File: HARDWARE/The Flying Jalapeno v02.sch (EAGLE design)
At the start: 96 parts, among them Q2 MMBT2222A, Q3 NDP6020P, Q4 MMBT2222A, Q5 NDP6020P, Q6 BSS138, 200mA/50V, Q7 BSS138, 200mA/50V, U1 ATMEGA2560AU, U2 LM1117, U3 LM1117, U4 LM1117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

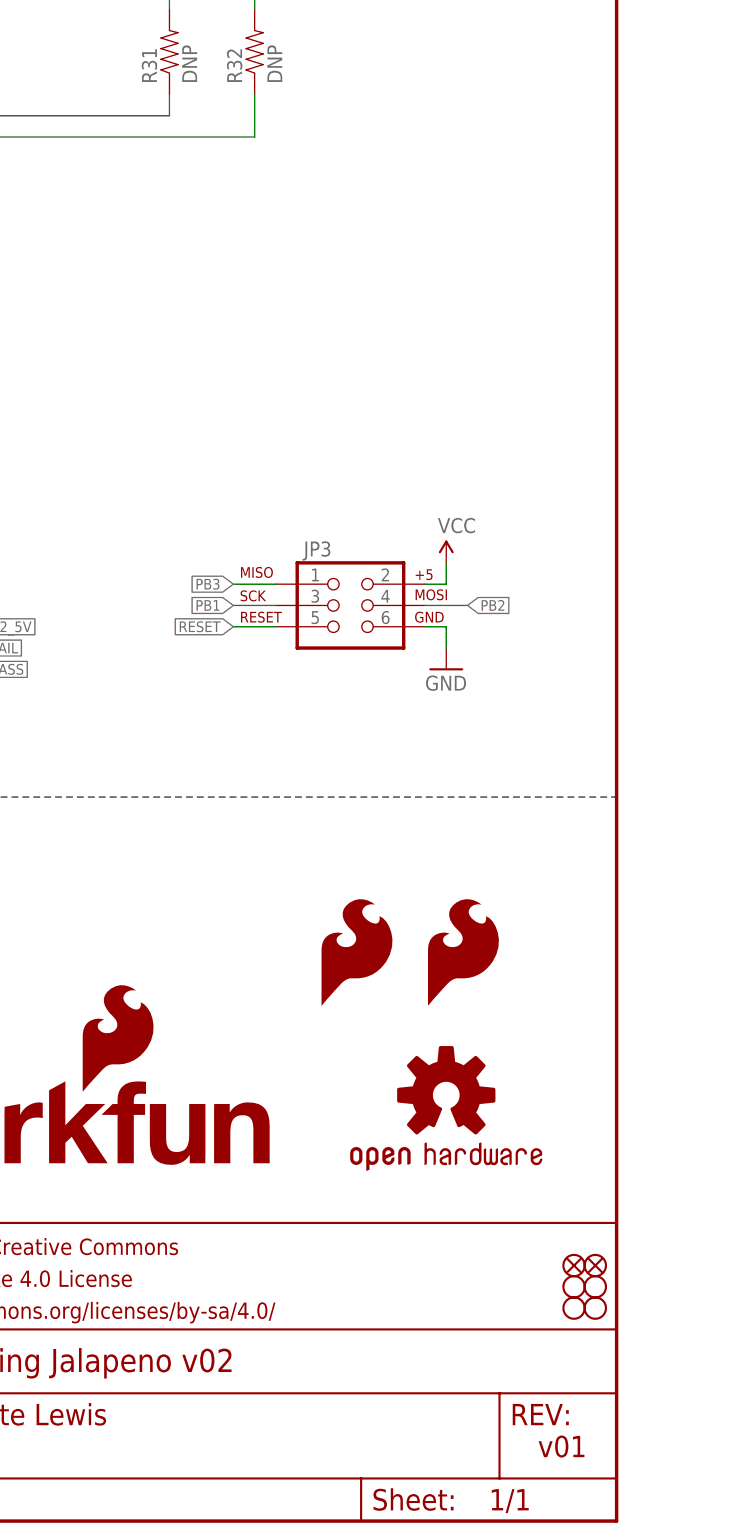
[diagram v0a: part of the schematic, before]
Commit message: added in PCA9306 for I2C - still not netted or routed
also added ignore for lock files
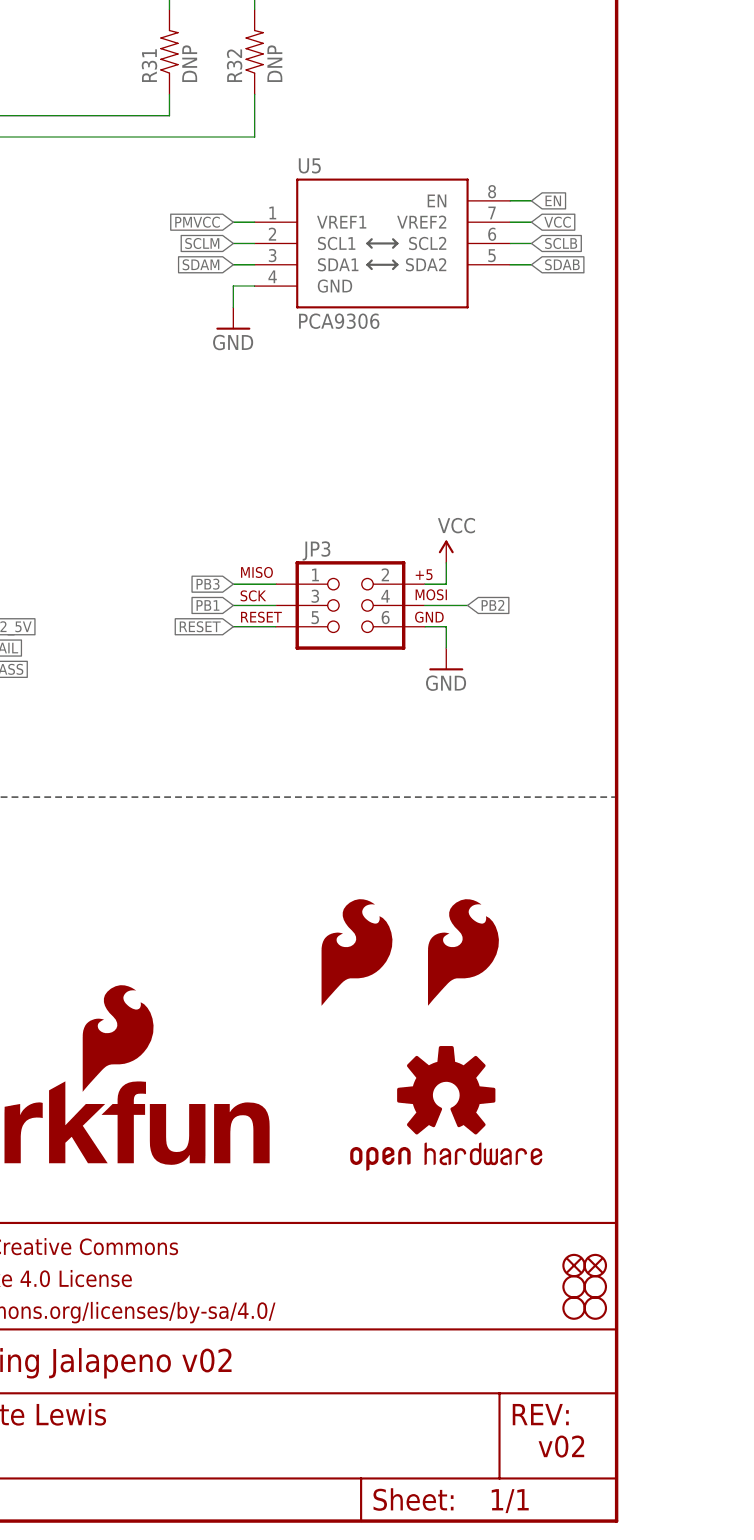
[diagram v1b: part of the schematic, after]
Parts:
- added U5: PCA9306, SparkFun-DigitalIC:PCA9306PCA9306DC-1:1
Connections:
- new net EN: U5.EN
- new net PMVCC: U5.VREF1
- new net SCLB: U5.SCL2
- new net SCLM: U5.SCL1
- new net SDAB: U5.SDA2
- new net SDAM: U5.SDA1
- net GND: now also U5.GND
- net VCC: now also U5.VREF2
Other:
- note added: "v02"
- note removed: "v01"
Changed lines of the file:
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@@
 <?xml version="1.0" encoding="utf-8"?>
 <!DOCTYPE eagle SYSTEM "eagle.dtd">
-<eagle version="7.3.0">
+<eagle version="7.5.0">
 <drawing>
 <settings>
@@
 <layer number="113" name="IDFDebug" color="4" fill="1" visible="yes" active="yes"/>
 <layer number="114" name="Badge_Outline" color="11" fill="1" visible="no" active="no"/>
+<layer number="115" name="ReferenceISLANDS" color="7" fill="1" visible="yes" active="yes"/>
 <layer number="116" name="Patch_BOT" color="9" fill="4" visible="yes" active="yes"/>
 <layer number="118" name="Rect_Pads" color="7" fill="1" visible="yes" active="yes"/>
@@
 </class>
 <class number="2" name="POWER" width="0.2032" drill="0">
+</class>
+<class number="10" name="12_mil" width="0.3048" drill="0.381">
+</class>
+<class number="11" name="15_mil" width="0.381" drill="0.381">
 </class>
 </classes>
@@
 <part name="R40" library="SparkFun-Resistors" deviceset="470OHM1/10W1%(0603)" device="" value="470"/>
 <part name="LOGO2" library="SparkFun-Aesthetics" deviceset="SFE_LOGO_FLAME" device=".3_INCH"/>
+<part name="U5" library="SparkFun-DigitalIC" deviceset="PCA9306" device="PCA9306DC-1:1" value="PCA9306"/>
+<part name="GND7" library="SparkFun" deviceset="GND" device=""/>
 </parts>
 <sheets>
@@
 <text x="200.66" y="269.24" size="3.81" layer="97">MICRO</text>
 <text x="354.33" y="11.43" size="2.54" layer="94">Pete Lewis</text>
-<text x="422.402" y="7.62" size="2.54" layer="94">v01</text>
+<text x="422.402" y="7.62" size="2.54" layer="94">v02</text>
 <text x="144.78" y="274.32" size="1.27" layer="97">RAW SPLIT</text>
 <text x="284.48" y="96.52" size="1.778" layer="97">ATMEGA2560V</text>
@@
 <instance part="R40" gate="G$1" x="76.2" y="109.22" rot="R90"/>
 <instance part="LOGO2" gate="G$1" x="396.24" y="60.96"/>
+<instance part="U5" gate="G$1" x="403.86" y="149.86"/>
+<instance part="GND7" gate="1" x="386.08" y="142.24"/>
 </instances>
 <busses>
@@
 <wire x1="414.02" y1="198.12" x2="411.48" y2="198.12" width="0.1524" layer="91"/>
 </segment>
+<segment>
+<pinref part="U5" gate="G$1" pin="GND"/>
+<wire x1="388.62" y1="147.32" x2="386.08" y2="147.32" width="0.1524" layer="91"/>
+<wire x1="386.08" y1="147.32" x2="386.08" y2="144.78" width="0.1524" layer="91"/>
+<pinref part="GND7" gate="1" pin="GND"/>
+</segment>
 </net>
 <net name="44/PT_CTRL" class="0">
@@
 <pinref part="R35" gate="G$1" pin="2"/>
 </segment>
+<segment>
+<pinref part="U5" gate="G$1" pin="VREF2"/>
+<wire x1="419.1" y1="154.94" x2="421.64" y2="154.94" width="0.1524" layer="91"/>
+<label x="421.64" y="154.94" size="1.27" layer="95" xref="yes"/>
+</segment>
 </net>
 <net name="RAW" class="1">
@@
 </segment>
 </net>
+<net name="SCLM" class="10">
+<segment>
+<pinref part="U5" gate="G$1" pin="SCL1"/>
+<wire x1="388.62" y1="152.4" x2="386.08" y2="152.4" width="0.1524" layer="91"/>
+<label x="386.08" y="152.4" size="1.27" layer="95" rot="R180" xref="yes"/>
+</segment>
+</net>
+<net name="EN" class="10">
+<segment>
+<pinref part="U5" gate="G$1" pin="EN"/>
+<wire x1="419.1" y1="157.48" x2="421.64" y2="157.48" width="0.1524" layer="91"/>
+<label x="421.64" y="157.48" size="1.27" layer="95" xref="yes"/>
+</segment>
+</net>
+<net name="SCLB" class="10">
+<segment>
+<pinref part="U5" gate="G$1" pin="SCL2"/>
+<wire x1="419.1" y1="152.4" x2="421.64" y2="152.4" width="0.1524" layer="91"/>
+<label x="421.64" y="152.4" size="1.27" layer="95" xref="yes"/>
+</segment>
+</net>
+<net name="SDAM" class="10">
+<segment>
+<pinref part="U5" gate="G$1" pin="SDA1"/>
+<wire x1="388.62" y1="149.86" x2="386.08" y2="149.86" width="0.1524" layer="91"/>
+<label x="386.08" y="149.86" size="1.27" layer="95" rot="R180" xref="yes"/>
+</segment>
+</net>
+<net name="SDAB" class="10">
+<segment>
+<pinref part="U5" gate="G$1" pin="SDA2"/>
+<wire x1="419.1" y1="149.86" x2="421.64" y2="149.86" width="0.1524" layer="91"/>
+<label x="421.64" y="149.86" size="1.27" layer="95" xref="yes"/>
+</segment>
+</net>
+<net name="PMVCC" class="10">
+<segment>
+<pinref part="U5" gate="G$1" pin="VREF1"/>
+<wire x1="388.62" y1="154.94" x2="386.08" y2="154.94" width="0.1524" layer="91"/>
+<label x="386.08" y="154.94" size="1.27" layer="95" rot="R180" xref="yes"/>
+</segment>
+</net>

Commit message: Placed/routed the PCA9306 into the design
Still some silk labeling to do, and check that GND pours are as good as
they can flow.
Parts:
- removed R31, R32: DNP, SparkFun-Resistors:10KOHM-1/10W-1%(0603)0603
- added C12: 10uF, SparkFun-Capacitors:10UF-6.3V-20%(0603)(TANT)"
- added C20: 10nF, SparkFun-Capacitors:10NF-0603-50V-10%
- added C7: 0.1uF, SparkFun-Capacitors:0.1UF-25V(+80/-20%)(0603)
- added TP1: TEST-POINT3, SparkFun-Passives:TEST-POINT3
- added U6: 3.3V MIC5205, SparkFun-PowerIC:MIC52053.3V
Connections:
- removed net EN: U5.EN
- removed net PMVCC: U5.VREF1
- removed net SCL: JP4.21(SCL/INT2), R32.1, U1.(SCL/INT0)PD0
- removed net SCLB: U5.SCL2
- removed net SCLM: U5.SCL1
- removed net SDA: JP4.20(SDA/INT3), R31.1, U1.(SDA/INT1)PD1
- removed net SDAB: U5.SDA2
- removed net SDAM: U5.SDA1
- new net 3.3V: C12.+, C7.1, TP1.1, U5.VREF1, U6.OUT
- new net EN_I2C: U1.(ICP1)PD4, U5.EN
- new net N$2: U1.(SDA/INT1)PD1, U5.SDA2
- new net N$27: U1.(SCL/INT0)PD0, U5.SCL2
- new net N$28: C20.1, U6.BP
- new net SCL1: JP4.21(SCL/INT2), U5.SCL1
- new net SDA1: JP4.20(SDA/INT3), U5.SDA1
- net GND: now also C12.-, C20.2, C7.2, U6.GND
- net RAW: now also U6.EN, U6.IN
- net VCC: no longer R31.2, R32.2
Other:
- note added: "1-3.6V"
- note added: "1.8-5V"
- note added: "3.3V Source for PCA9306"
- note added: "Max Current Output: 150mA"
- note added: "Max Voltage Input: 16VDC"
- moved on the sheet: JP2, Q6, Q7, R17, R34, R35, R41, U5

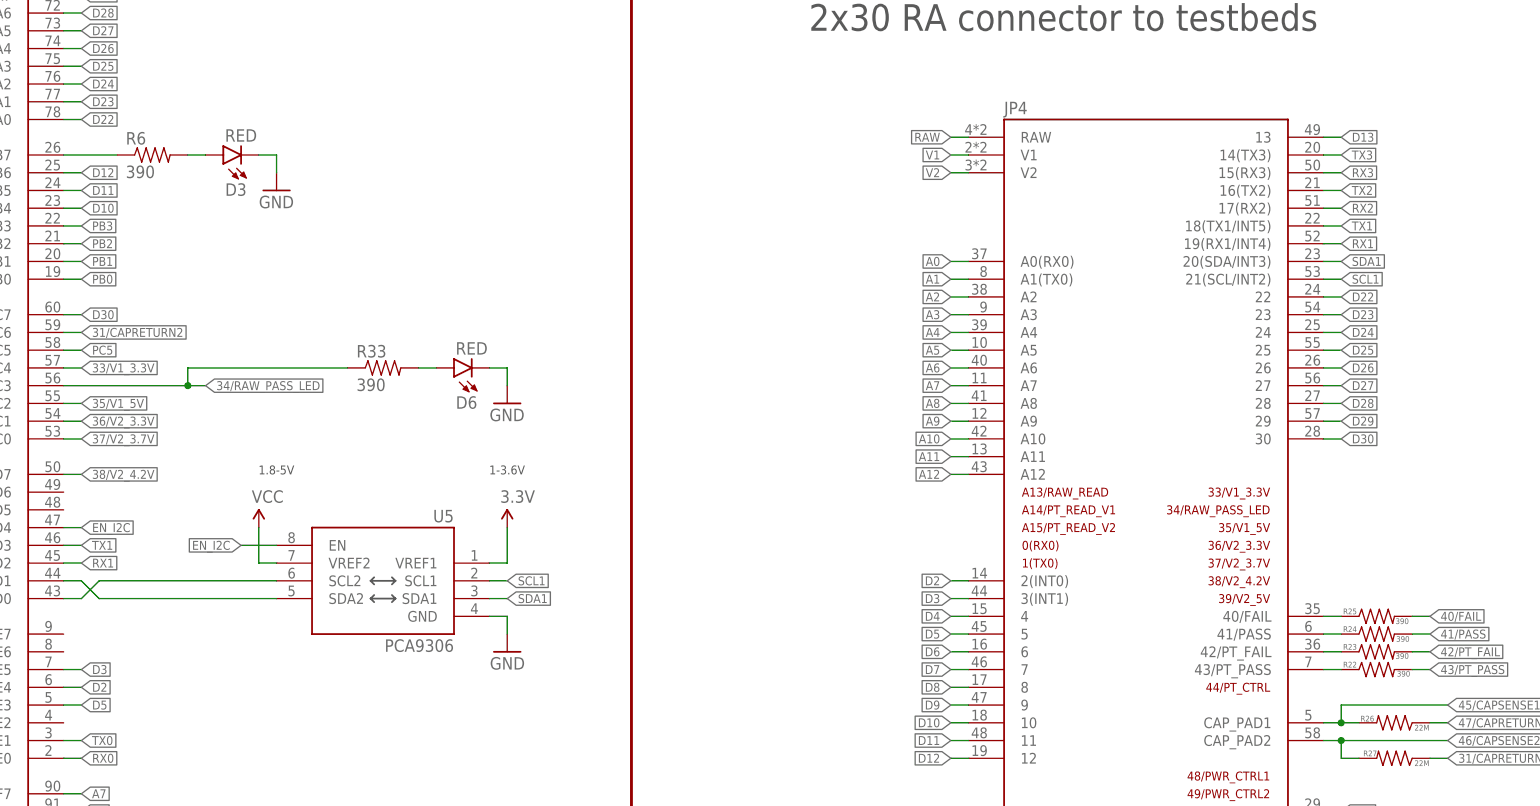
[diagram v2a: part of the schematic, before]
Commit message: finished up routing and adjusted silk
Added/updated silk to:
Led resistors (stat and 4 others)- now are 1K
MIC5205 3.3V vreg
10uF pol cap
10nF bypass cap - near vreg
PCA9306
0.1uF cap near PCA9306
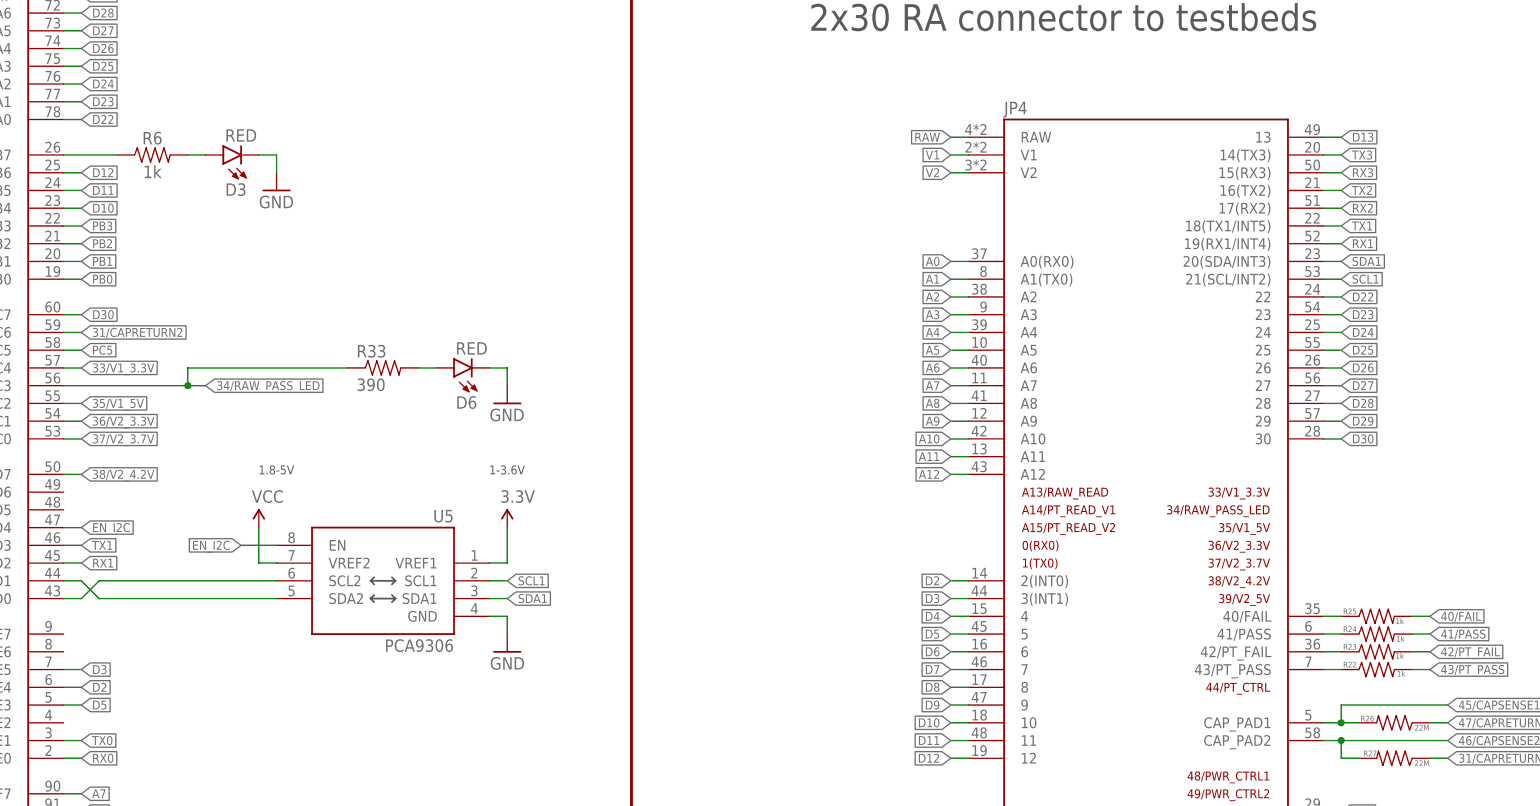
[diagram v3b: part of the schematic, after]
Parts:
- R22, R23, R24, R25, R6: value 390 -> 1k; device SparkFun-Resistors:390OHM1/10W1%(0603) -> SparkFun-Resistors:1KOHM-0603-1/10W-1%
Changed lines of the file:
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@@
 <part name="GND3" library="SparkFun" deviceset="GND" device=""/>
 <part name="C1" library="SparkFun-Capacitors" deviceset="0.1UF-25V(+80/-20%)(0603)" device="" value="0.1uF"/>
-<part name="R6" library="SparkFun-Resistors" deviceset="390OHM1/10W1%(0603)" device="" value="390"/>
+<part name="R6" library="SparkFun-Resistors" deviceset="1KOHM" device="-0603-1/10W-1%" value="1k"/>
 <part name="D3" library="SparkFun-LED" deviceset="LED-RED" device="1206" value="RED"/>
 <part name="GND8" library="SparkFun" deviceset="GND" device=""/>
@@
 <part name="SJ3" library="SparkFun-Passives" deviceset="JUMPER-PAD-3-2OF3_NC_BY_PASTE" device="" value=""/>
 <part name="SJ4" library="SparkFun-Passives" deviceset="JUMPER-PAD-3-2OF3_NC_BY_PASTE" device="" value=""/>
-<part name="R22" library="SparkFun-Resistors" deviceset="390OHM1/10W1%(0603)" device="" value="390"/>
-<part name="R23" library="SparkFun-Resistors" deviceset="390OHM1/10W1%(0603)" device="" value="390"/>
-<part name="R24" library="SparkFun-Resistors" deviceset="390OHM1/10W1%(0603)" device="" value="390"/>
-<part name="R25" library="SparkFun-Resistors" deviceset="390OHM1/10W1%(0603)" device="" value="390"/>
+<part name="R22" library="SparkFun-Resistors" deviceset="1KOHM" device="-0603-1/10W-1%" value="1k"/>
+<part name="R23" library="SparkFun-Resistors" deviceset="1KOHM" device="-0603-1/10W-1%" value="1k"/>
+<part name="R24" library="SparkFun-Resistors" deviceset="1KOHM" device="-0603-1/10W-1%" value="1k"/>
+<part name="R25" library="SparkFun-Resistors" deviceset="1KOHM" device="-0603-1/10W-1%" value="1k"/>
 <part name="R26" library="SparkFun-Resistors" deviceset="22MOHM-1/10W-10%(0603)" device="" value="22M"/>
 <part name="R27" library="SparkFun-Resistors" deviceset="22MOHM-1/10W-10%(0603)" device="" value="22M"/>
